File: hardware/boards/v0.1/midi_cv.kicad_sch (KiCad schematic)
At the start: 23 parts, among them J10 MIDI_OUT/THRU, J11 MIDI_IN, U19 TLP2362TPR_E, U30 TS5A23159RSE, U34 TS5A23159RSE, U35 TS5A23159RSE

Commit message: feat: various schematic organization
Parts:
- removed C28, C40: 0.1uF, Capacitor_SMD:C_0201_0603Metric, symbol Device:C_Small
- removed R20, R41: 10k, Resistor_SMD:R_0201_0603Metric, symbol Device:R
- removed U30, U34: TS5A23159RSE, Package_DFN_QFN:Texas_R-PUQFN-N10, symbol Analog_Switch:TS5A23159RSE
- added R18, R43, R44, R47, R48, R49: 24.9k, symbol Device:R
- added R45, R46: 100k, symbol Device:R
- added U27, U36: MCP6002-xMC, Package_DFN_QFN:DFN-8-1EP_3x2mm_P0.5mm_EP1.75x1.45mm, symbol Amplifier_Operational:MCP6002-xMC
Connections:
- net +3.3V: now also U27.8 (V+), U36.8 (V+)
- net GND: now also U27.3 (+), U27.4 (V-), U27.5 (+), U27.9 (V-), U36.3 (+), U36.4 (V-), U36.5 (+), U36.9 (V-)
- net at J11.R: now also FB4.2
- net at FB3.2: now also J11.T
- net at FB2.1: now also J10.R
- net at J10.T: now also FB1.1
- new net: R43.1, R45.2, U27.6 (-)
- new net: R18.1, R43.2, U27.7
- new net: R47.2, R48.1, U36.7
- new net: R48.2, R49.1, U36.2 (-)
- new net: R18.2, R44.1, U27.2 (-)
- new net: R44.2, U27.1
- new net: R49.2, U36.1
- new net: R46.2, R47.1, U36.6 (-)
- new net CV_RAW_A: R45.1
- new net CV_RAW_B: R46.1
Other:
- note added: "+/-12v to 0-3.3v"
- note added: "CV Input by Émilie Gillet of Mutable Instruments https://wiki.synthdiy.com/building-blocks/cv-input-to-microcontroller/"
- note added: "CV Level Shifting"
- note added: "MIDI IN"
- note added: "MIDI OUT/THRU"
- note added: "MIDI input, passthrough, or CV"
- note added: "MIDI output, passthrough, or CV"
- note added: "TODO: 5v boost converter"
- note added: "TODO: MUX with 5v tollerant analog output"
- moved on the sheet: C39, C41, C43, D18, FB1, FB2, FB3, FB4, J10, J11, R12, R3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

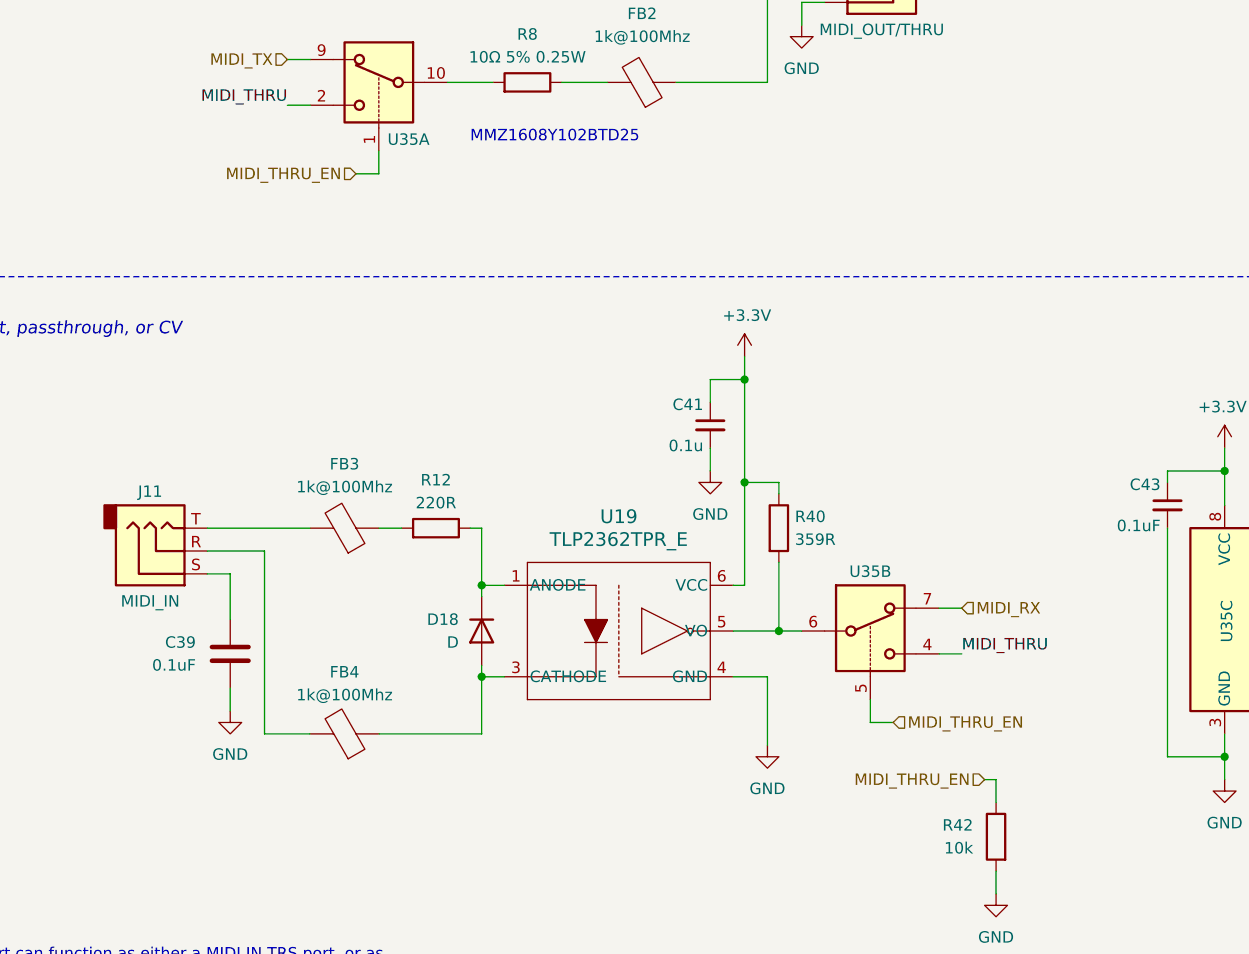
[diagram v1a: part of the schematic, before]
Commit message: feat: schematic organization, MIDI port routing
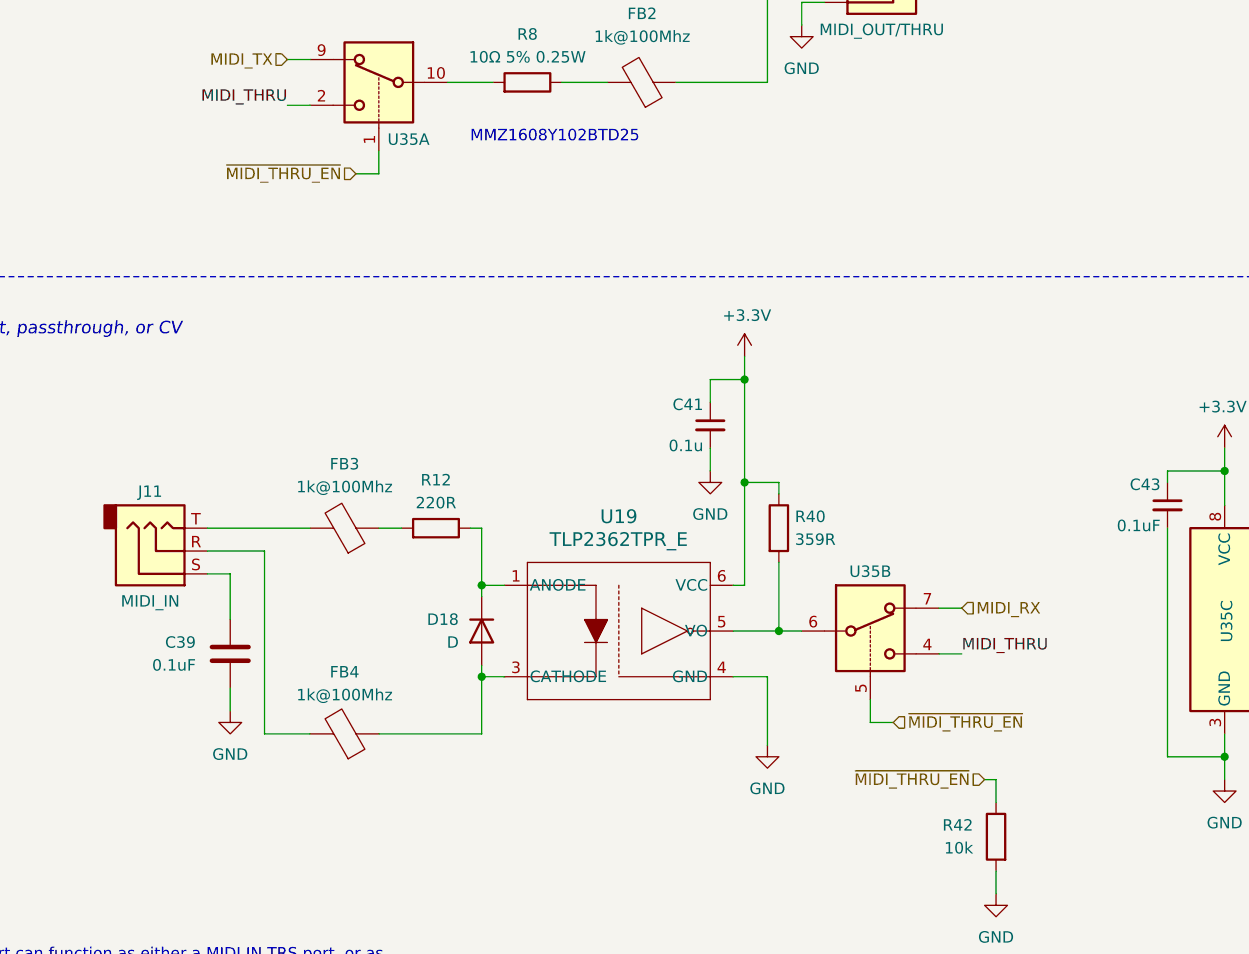
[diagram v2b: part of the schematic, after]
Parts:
- C41: footprint (none) -> Capacitor_SMD:C_0603_1608Metric
- C43: footprint Capacitor_SMD:C_0201_0603Metric -> Capacitor_SMD:C_0603_1608Metric
- D18: footprint (none) -> Diode_SMD:D_0603_1608Metric
- R18, R40, R43, R44, R45, R46, R47, R48, R49: footprint (none) -> Resistor_SMD:R_0603_1608Metric
- R42: footprint Resistor_SMD:R_0201_0603Metric -> Resistor_SMD:R_0603_1608Metric
- U19: footprint 11-4L1S_TOS -> pocket_synth:TLP2362TPR_E
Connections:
- net MIDI_THRU_EN renamed ~{MIDI_THRU_EN}

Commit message: feat: route audio components
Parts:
- C39: footprint (none) -> Capacitor_SMD:C_0603_1608Metric

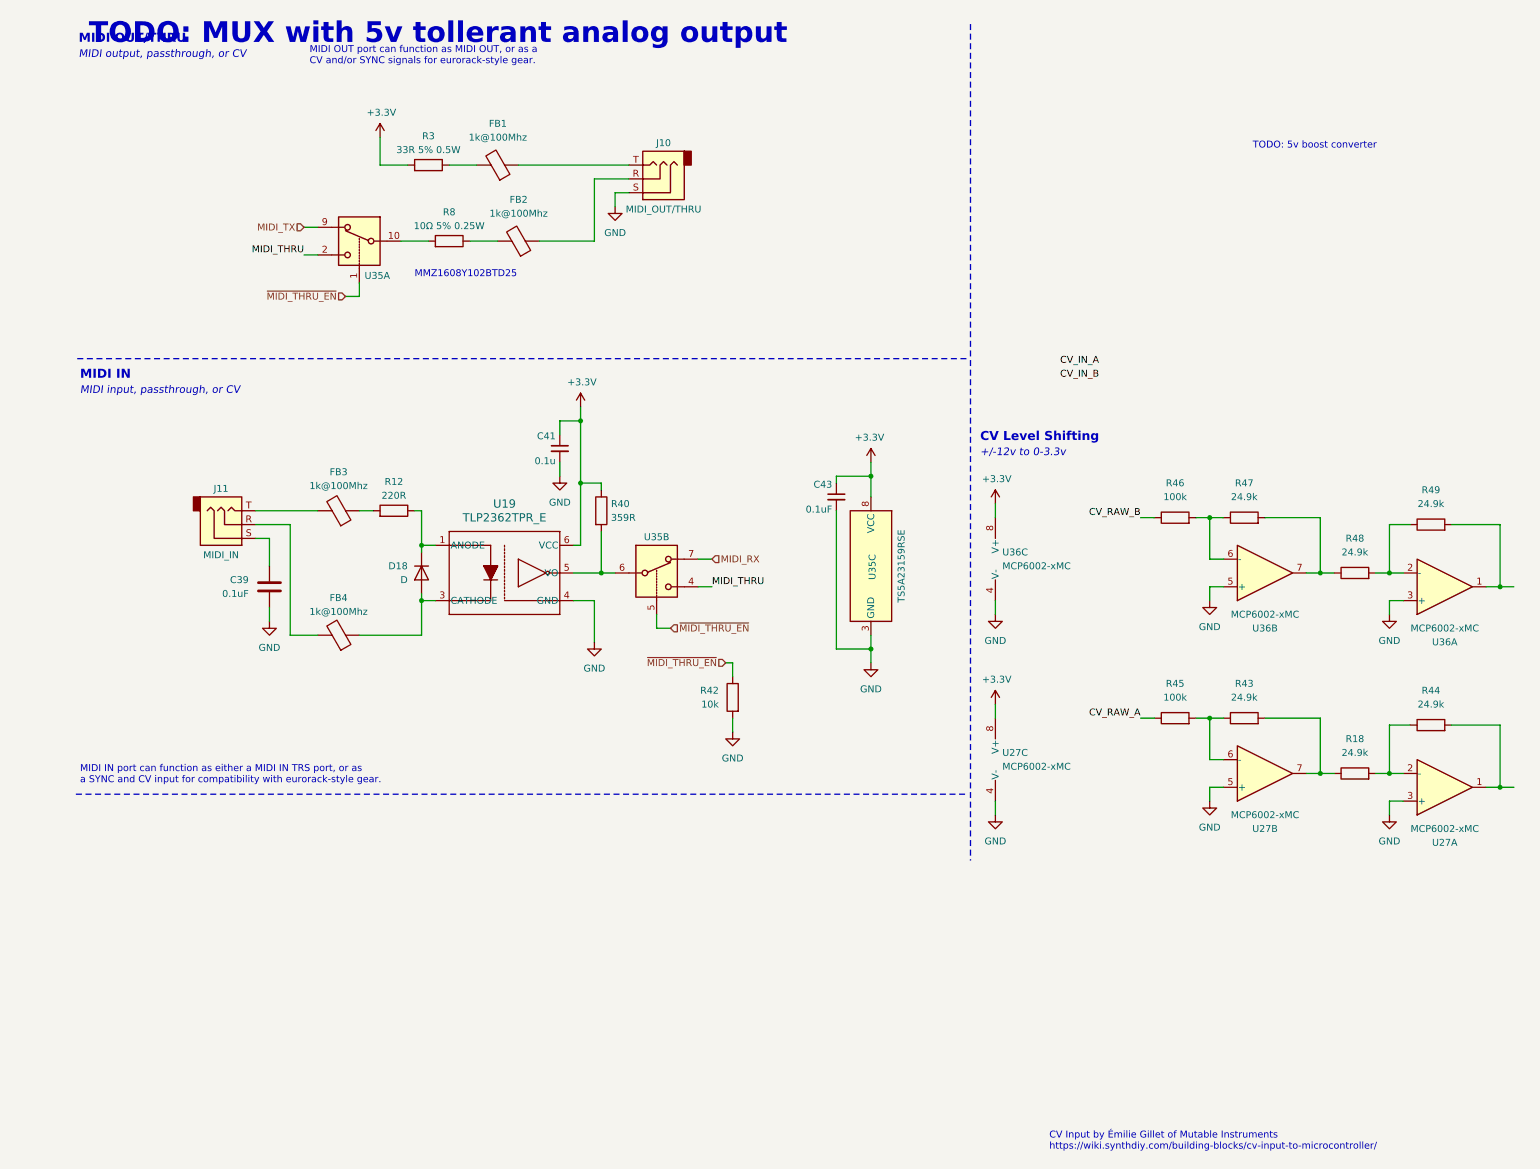
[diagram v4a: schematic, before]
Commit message: fix: I2C routing for keypad
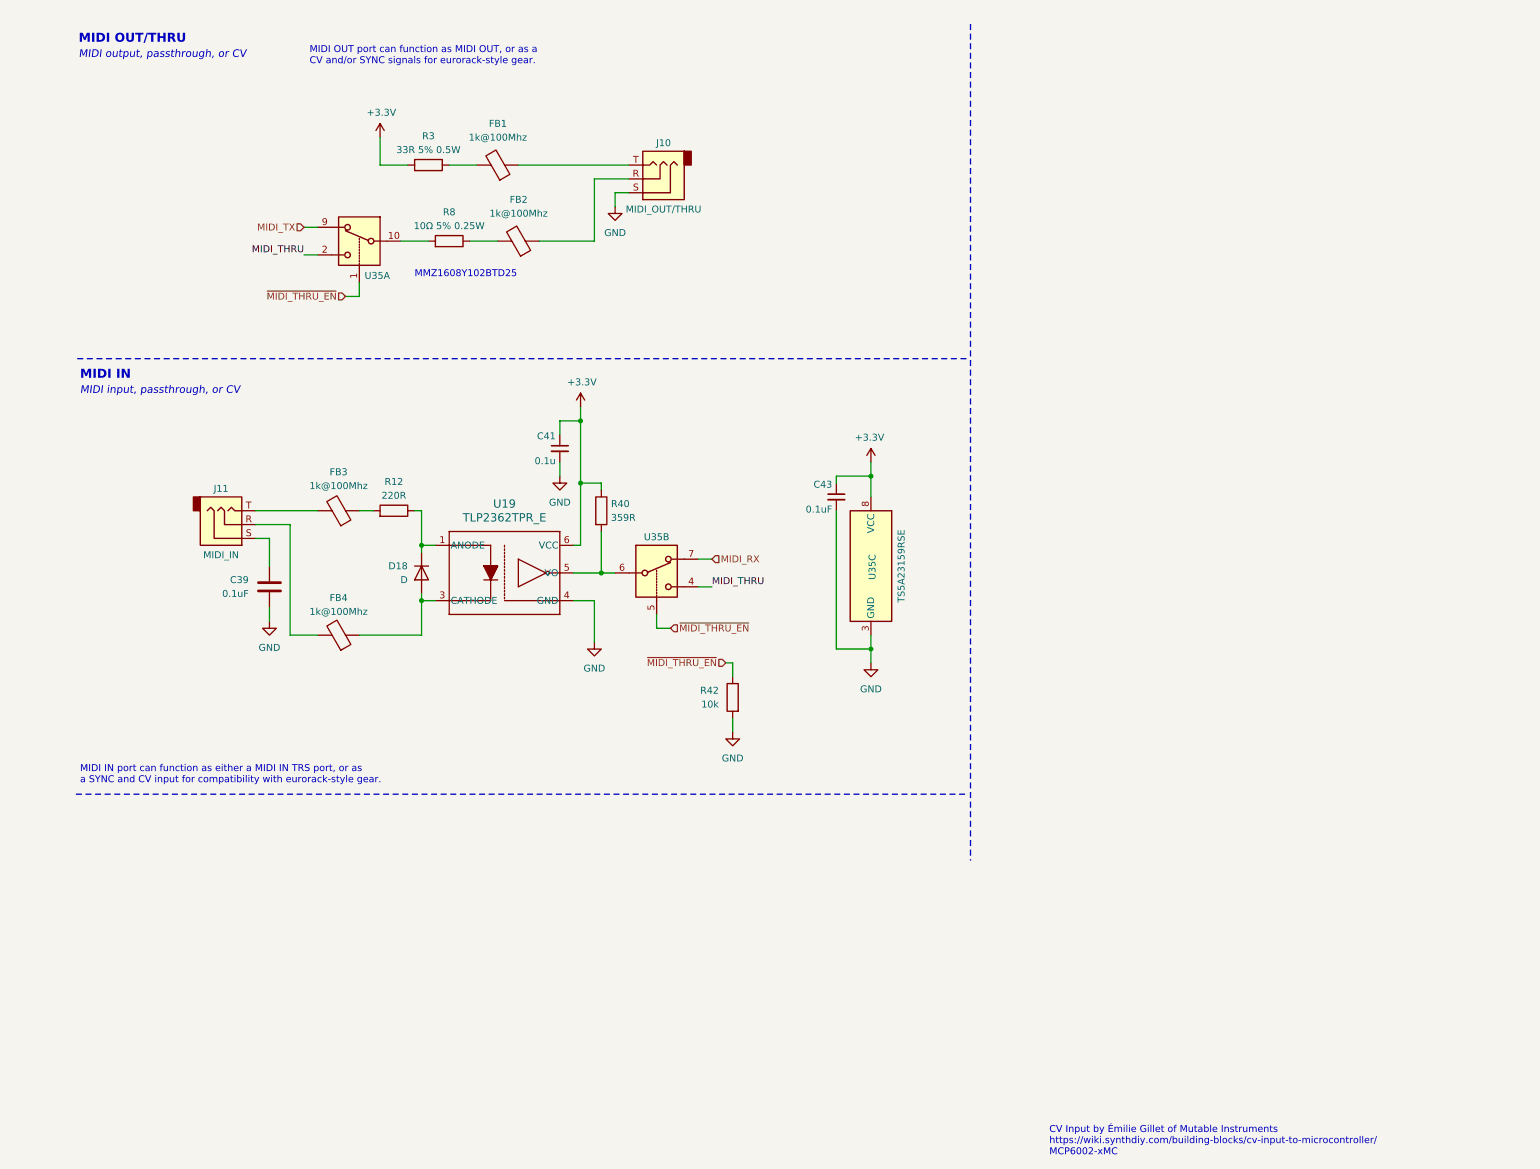
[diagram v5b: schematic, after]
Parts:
- removed R18, R43, R44, R47, R48, R49: 24.9k, Resistor_SMD:R_0603_1608Metric, symbol Device:R
- removed R45, R46: 100k, Resistor_SMD:R_0603_1608Metric, symbol Device:R
- removed U27, U36: MCP6002-xMC, Package_DFN_QFN:DFN-8-1EP_3x2mm_P0.5mm_EP1.75x1.45mm, symbol Amplifier_Operational:MCP6002-xMC
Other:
- note added: "CV Input by Émilie Gillet of Mutable Instruments https://wiki.synthdiy.com/building-blocks/cv-input-to-microcontroller/ MCP6002-xMC"
- note removed: "+/-12v to 0-3.3v"
- note removed: "CV Input by Émilie Gillet of Mutable Instruments https://wiki.synthdiy.com/building-blocks/cv-input-to-microcontroller/"
- note removed: "CV Level Shifting"
- note removed: "TODO: 5v boost converter"
- note removed: "TODO: MUX with 5v tollerant analog output"

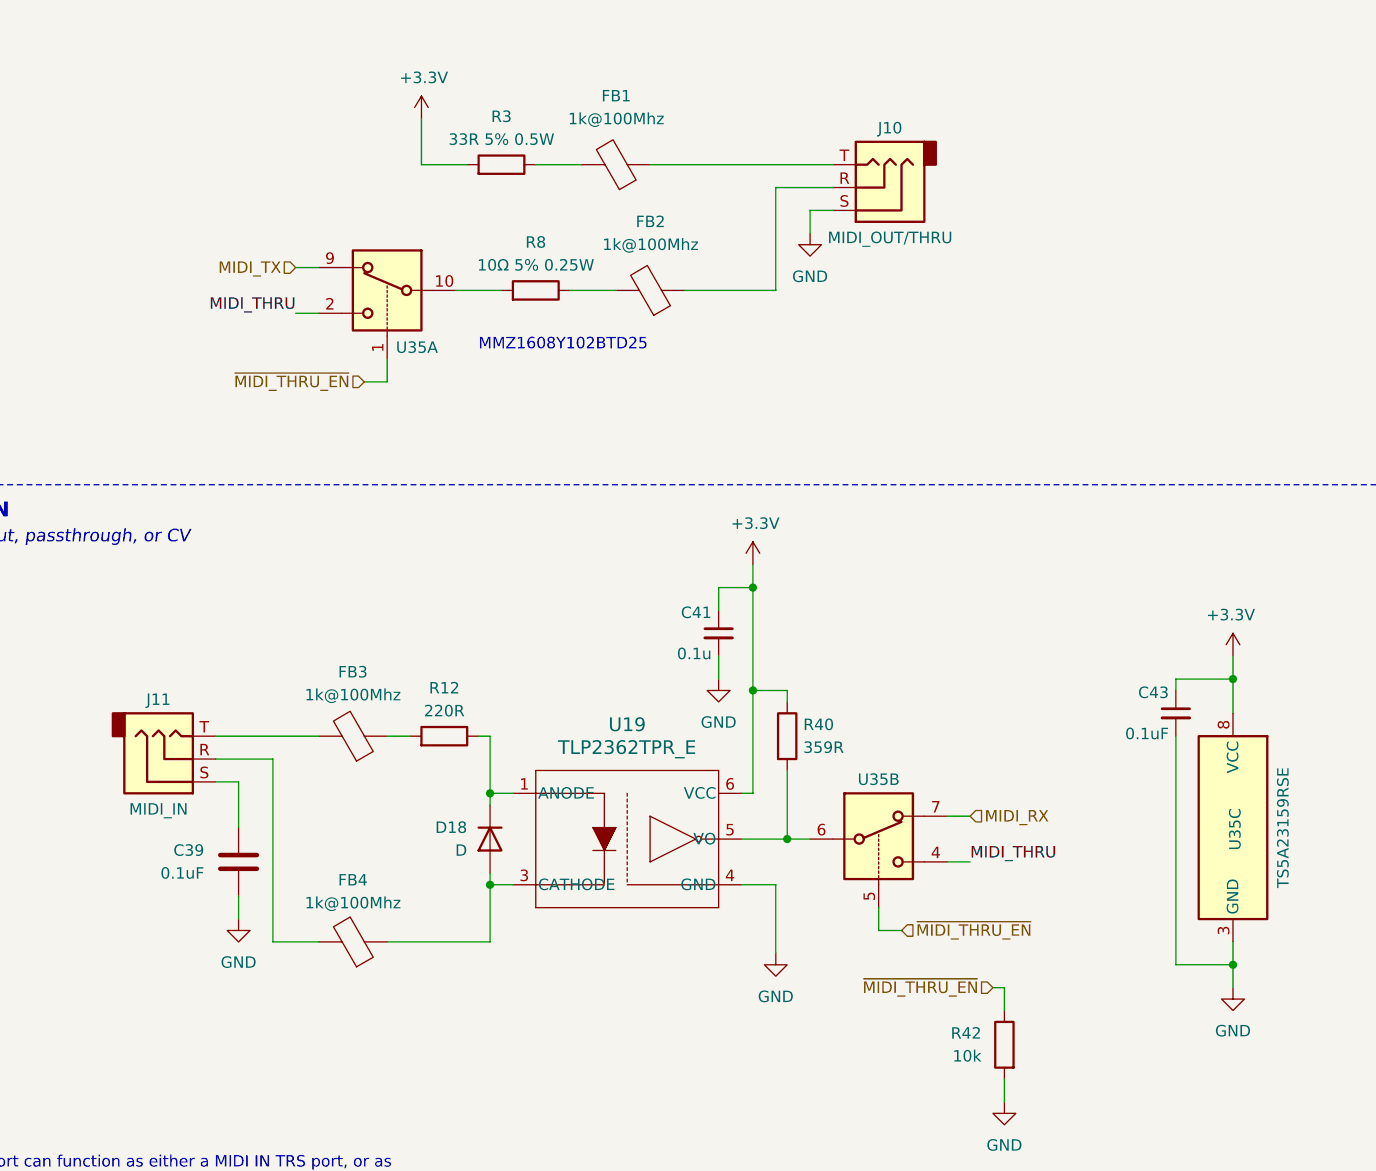
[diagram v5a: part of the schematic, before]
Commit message: feat: add test points and top and bottom ground pours
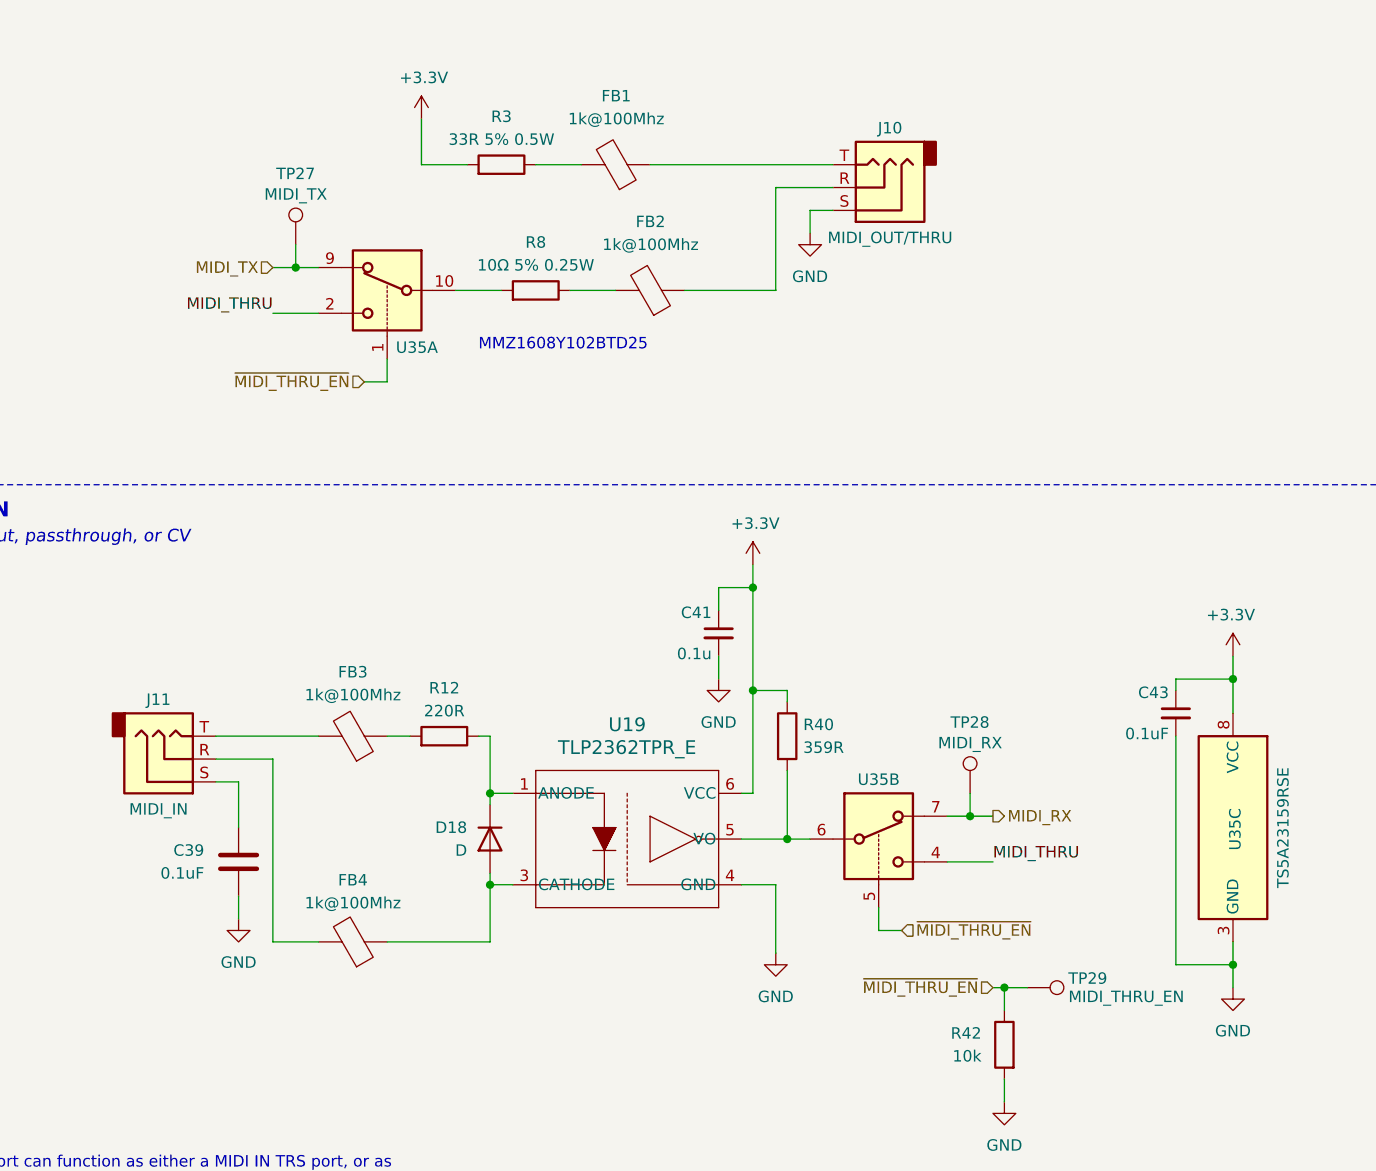
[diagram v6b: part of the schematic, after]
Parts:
- added TP27: MIDI_TX, TestPoint:TestPoint_Pad_D1.0mm, symbol Connector:TestPoint
- added TP28: MIDI_RX, TestPoint:TestPoint_Pad_D1.0mm, symbol Connector:TestPoint
- added TP29: MIDI_THRU_EN, TestPoint:TestPoint_Pad_D1.0mm, symbol Connector:TestPoint
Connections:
- net MIDI_RX: now also TP28.1
- net MIDI_TX: now also TP27.1
- net ~{MIDI_THRU_EN}: now also TP29.1
